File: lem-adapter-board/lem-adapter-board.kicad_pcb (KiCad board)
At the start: 2 copper layers, 40 x 130.5 mm, 69 parts, among them J1 Conn_01x04, J2 Conn_01x04, J3 Conn_01x04, J4 Conn_01x04, J5 Conn_01x04, J6 Conn_01x04, J7 Conn_01x04, J8 Conn_01x04, J9 Conn_02x10_Odd_Even

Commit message: Changed order in lem adapter connector
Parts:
- removed the REF** at (54.1, 56.1)
- removed the REF** at (54.1, 93.6)
- added REF**: MountingHole_3.2mm_M3, MountingHole:MountingHole_3.2mm_M3, F.Cu at (53.6, 55.7)
- added REF**: MountingHole_3.2mm_M3, MountingHole:MountingHole_3.2mm_M3, F.Cu at (53.6, 92.7)
- D2, F1: moved to F.Cu
- moved D2 13.5 mm to (71.6, 15.8), turned to 180 degrees
- moved F1 8.24 mm to (71.5, 18.7), turned to 0 degrees
- moved D3 0.82 mm to (46.2, 19.1), turned to 180 degrees
- moved F2 0.79 mm to (46.4, 16.0)
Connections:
- D2 pad 1: GND -> +VCC
- D2 pad 2: -VCC -> GND
- D3 pad 1: +VCC -> GND
- D3 pad 2: GND -> -VCC
- F1 pad 1: -VDD -> +VDD
- F1 pad 2: -VCC -> +VCC
- F2 pad 1: +VDD -> -VDD
- F2 pad 2: +VCC -> -VCC
- J1 pad 1: +VCC -> GND
- J1 pad 3: GND -> -VCC
- J1 pad 4: -VCC -> +VCC
- J2 pad 1: +VCC -> GND
- J2 pad 3: GND -> -VCC
- J2 pad 4: -VCC -> +VCC
- J3 pad 1: +VCC -> GND
- J3 pad 3: GND -> -VCC
- J3 pad 4: -VCC -> +VCC
- J4 pad 1: +VCC -> GND
- J4 pad 3: GND -> -VCC
- J4 pad 4: -VCC -> +VCC
- J5 pad 1: +VCC -> GND
- J5 pad 3: GND -> -VCC
- J5 pad 4: -VCC -> +VCC
- J6 pad 1: +VCC -> GND
- J6 pad 3: GND -> -VCC
- J6 pad 4: -VCC -> +VCC
- J8 pad 1: -VDD -> +VDD
- J8 pad 4: +VDD -> -VDD
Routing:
- net +VCC: track 182.1 -> 234.2 mm
- net -VCC: track 208.1 -> 180.3 mm
- net -VDD: track 3.89 -> 4.88 mm
- net +VDD: track 3.54 -> 4.17 mm

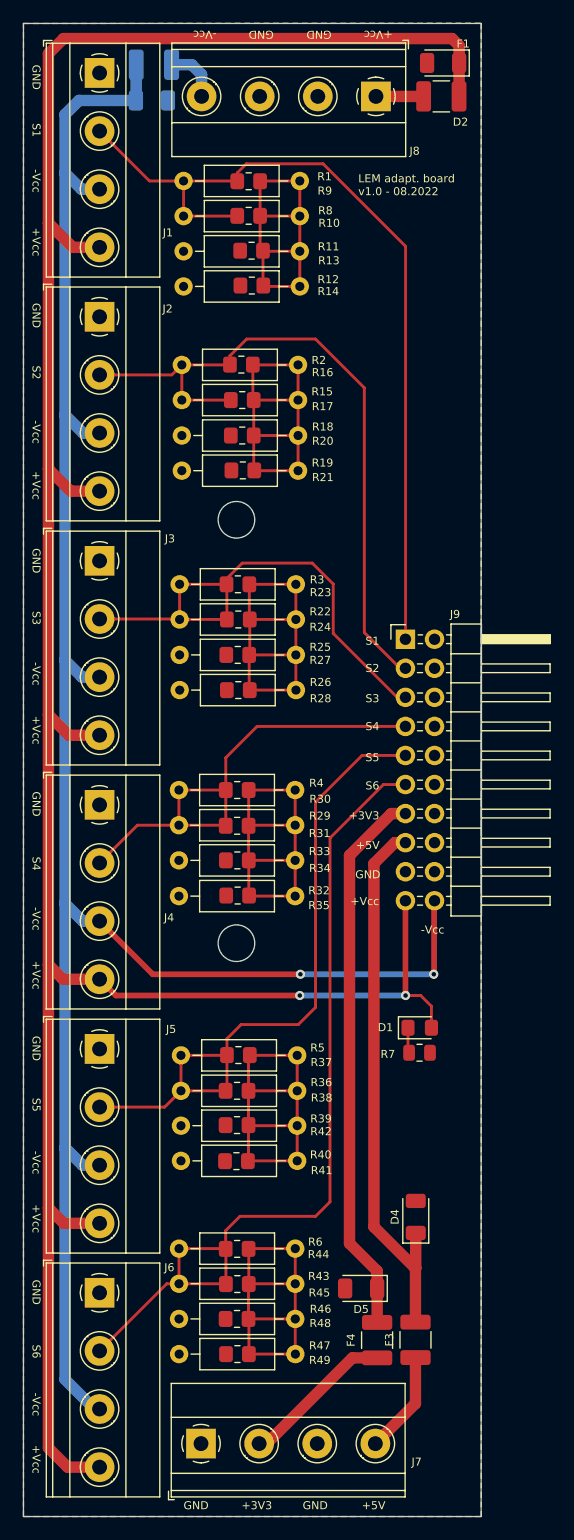
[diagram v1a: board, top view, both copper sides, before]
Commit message: Generated gerber files for lem adapter board
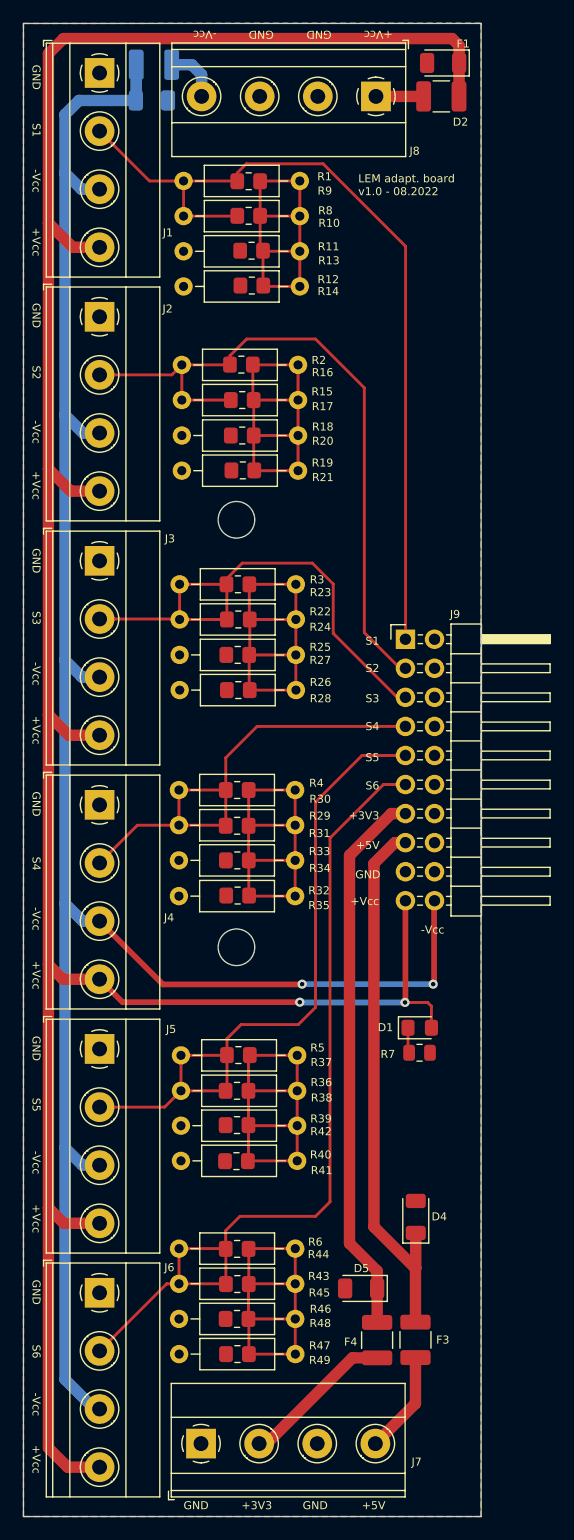
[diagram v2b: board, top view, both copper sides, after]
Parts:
- moved REF** 0.36 mm to (53.6, 93.1)
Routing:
- net -VCC: track 180.3 -> 181.5 mm
- net +VCC: track 234.2 -> 234.8 mm
